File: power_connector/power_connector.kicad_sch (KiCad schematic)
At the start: 2 parts, among them J1 Conn_01x04_Socket, J2 Conn_01x02_Pin

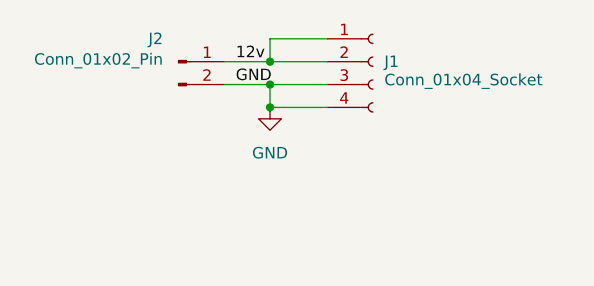
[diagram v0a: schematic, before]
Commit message: mounting holes and board outline
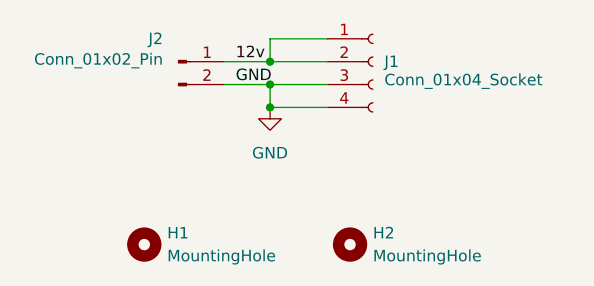
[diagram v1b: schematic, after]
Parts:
- added H1, H2: MountingHole, MountingHole:MountingHole_2.2mm_M2, symbol Mechanical:MountingHole
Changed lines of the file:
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@@
+	)
+	(symbol
+		(lib_id "Mechanical:MountingHole")
+		(at 93.98 116.84 0)
+		(unit 1)
+		(body_style 1)
+		(exclude_from_sim no)
+		(in_bom no)
+		(on_board yes)
+		(in_pos_files yes)
+		(dnp no)
+		(fields_autoplaced yes)
+		(property "Reference" "H1"
+			(at 96.52 115.5699 0)
+			(show_name no)
+			(do_not_autoplace no)
+			(effects
+				(font
+					(size 1.27 1.27)
+				)
+				(justify left)
+			)
+		)
+		(property "Value" "MountingHole"
+			(at 96.52 118.1099 0)
+			(show_name no)
+			(do_not_autoplace no)
+			(effects
+				(font
+					(size 1.27 1.27)
+				)
+				(justify left)
+			)
+		)
+		(property "Footprint" "MountingHole:MountingHole_2.2mm_M2"
+			(at 93.98 116.84 0)
+			(hide yes)
+			(show_name no)
+			(do_not_autoplace no)
+			(effects
+				(font
+					(size 1.27 1.27)
+				)
+			)
+		)
+		(property "Datasheet" ""
+			(at 93.98 116.84 0)
+			(hide yes)
+			(show_name no)
+			(do_not_autoplace no)
+			(effects
+				(font
+					(size 1.27 1.27)
+				)
+			)
+		)
+		(property "Description" "Mounting Hole without connection"
+			(at 93.98 116.84 0)
+			(hide yes)
+			(show_name no)
+			(do_not_autoplace no)
+			(effects
+				(font
+					(size 1.27 1.27)
+				)
+			)
+		)
+		(instances
+			(project "power_connector"
+				(path "/269ff752-62b3-42f1-822f-1087e9d8a6f4"
+					(reference "H1")
+					(unit 1)
+				)
+			)
+		)
 	)
 	(symbol
@@
 					(unit 1)
 				)
+			)
+		)
+	)
+	(symbol
+		(lib_id "Mechanical:MountingHole")
+		(at 116.84 116.84 0)
+		(unit 1)
+		(body_style 1)
+		(exclude_from_sim no)
+		(in_bom no)
+		(on_board yes)
+		(in_pos_files yes)
+		(dnp no)
+		(fields_autoplaced yes)
+		(property "Reference" "H2"
+			(at 119.38 115.5699 0)
+			(show_name no)
+			(do_not_autoplace no)
+			(effects
+				(font
+					(size 1.27 1.27)
+				)
+				(justify left)
+			)
+		)
+		(property "Value" "MountingHole"
+			(at 119.38 118.1099 0)
+			(show_name no)
+			(do_not_autoplace no)
+			(effects
+				(font
+					(size 1.27 1.27)
+				)
+				(justify left)
+			)
+		)
+		(property "Footprint" "MountingHole:MountingHole_2.2mm_M2"
+			(at 116.84 116.84 0)
+			(hide yes)
+			(show_name no)
+			(do_not_autoplace no)
+			(effects
+				(font
+					(size 1.27 1.27)
+				)
+			)
+		)
+		(property "Datasheet" ""
+			(at 116.84 116.84 0)
+			(hide yes)
+			(show_name no)
+			(do_not_autoplace no)
+			(effects
+				(font
+					(size 1.27 1.27)
+				)
+			)
+		)
+		(property "Description" "Mounting Hole without connection"
+			(at 116.84 116.84 0)
+			(hide yes)
+			(show_name no)
+			(do_not_autoplace no)
+			(effects
+				(font
+					(size 1.27 1.27)
+				)
+			)
+		)
+		(instances
+			(project "power_connector"
+				(path "/269ff752-62b3-42f1-822f-1087e9d8a6f4"
+					(reference "H2")
+					(unit 1)
+				)
